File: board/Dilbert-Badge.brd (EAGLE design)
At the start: 53 x 106.7 mm, 27 parts, among them IC1 MCP23017SO, J1 I2C, J2 UART, J6 IO_B, J7 IO_A, SW1 UP, SW2 DOWN, SW3 LEFT, SW4 RIGHT, SW5 A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

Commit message: Update board
[ci skip]
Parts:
- added R5, R6: 10K, adafruit:R0805
- R4: value (none) -> 10K
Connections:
- net LED_OUT renamed NEOPIXEL_OUT
- net N$10 renamed MOSI
- net N$11 renamed MISO
- net N$12 renamed TFT_CS
- net N$9 renamed SCK
- removed net LED_IN: J5.7, LED1.4-DIN, R4.2, X1.10
- new net NEOPIXEL: J5.7, LED1.4-DIN, R6.2, X1.10
- new net TFT_DC: J5.6, R4.1, X1.11
- net 3V3: now also R4.2, R5.2
- net GND: now also R6.1; no longer R4.1
- net GPIO2: no longer J5.6, X1.11
- net SCL: now also R5.1
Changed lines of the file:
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@@
 <element name="R2" library="adafruit" package="R0805" value="10K" x="41.91" y="64.77" rot="R270"/>
 <element name="R3" library="adafruit" package="R0805" value="10K" x="11.43" y="63.5" rot="R90"/>
-<element name="R4" library="adafruit" package="R0805" value="" x="12.7" y="54.61" rot="R90"/>
+<element name="R4" library="adafruit" package="R0805" value="10K" x="12.7" y="54.61" rot="R90"/>
 <element name="C1" library="SparkFun-Capacitors" package="0805-CAP" value="" x="10.16" y="59.69" rot="R90">
 <attribute name="PROD_ID" value="CAP-11330" x="10.16" y="59.69" size="1.778" layer="27" rot="R90" display="off"/>
 </element>
+<element name="R5" library="adafruit" package="R0805" value="10K" x="5.08" y="44.45" rot="R90"/>
+<element name="R6" library="adafruit" package="R0805" value="10K" x="5.08" y="36.83" rot="R270"/>
 </elements>
 <signals>
@@
 <contactref element="IC1" pad="10"/>
 <contactref element="SW8" pad="P$1"/>
-<contactref element="R4" pad="1"/>
 <contactref element="C1" pad="2"/>
+<contactref element="R6" pad="1"/>
 <wire x1="44.83" y1="32.93" x2="49.53" y2="33.02" width="0" layer="19" extent="1-1"/>
 <wire x1="33.4" y1="32.93" x2="44.83" y2="32.93" width="0" layer="19" extent="1-1"/>
@@
 <wire x1="15.24" y1="53.34" x2="16.51" y2="43.89" width="0" layer="19" extent="1-1"/>
 <wire x1="19.17" y1="54" x2="15.24" y2="53.34" width="0" layer="19" extent="16-16"/>
-<wire x1="6.35" y1="55.88" x2="15.24" y2="53.34" width="0" layer="19" extent="1-1"/>
-<wire x1="6.35" y1="59.69" x2="6.35" y2="55.88" width="0" layer="19" extent="1-1"/>
+<wire x1="10.16" y1="60.59" x2="15.24" y2="53.34" width="0" layer="19" extent="1-1"/>
+<wire x1="6.35" y1="59.69" x2="10.16" y2="60.59" width="0" layer="19" extent="1-1"/>
+<wire x1="6.35" y1="55.88" x2="6.35" y2="59.69" width="0" layer="19" extent="1-1"/>
 <wire x1="13.26" y1="21.59" x2="10.54" y2="32.93" width="0" layer="19" extent="1-1"/>
 <wire x1="19.61" y1="16.51" x2="13.26" y2="21.59" width="0" layer="19" extent="1-1"/>
@@
 <wire x1="41.2" y1="20.32" x2="44.83" y2="32.93" width="0" layer="19" extent="1-1"/>
 <wire x1="33.58" y1="12.7" x2="41.2" y2="20.32" width="0" layer="19" extent="1-1"/>
-<wire x1="12.7" y1="53.61" x2="13.26" y2="11.43" width="0" layer="19" extent="1-1"/>
-<wire x1="10.16" y1="60.59" x2="12.7" y2="53.61" width="0" layer="19" extent="1-1"/>
+<wire x1="5.08" y1="37.83" x2="13.26" y2="11.43" width="0" layer="19" extent="1-1"/>
 </signal>
 <signal name="BTN_U">
@@
 <contactref element="IC1" pad="12"/>
 <contactref element="SW8" pad="P$2"/>
+<contactref element="R5" pad="1"/>
 <wire x1="15.24" y1="60.96" x2="19.17" y2="60" width="0" layer="19" extent="16-16"/>
 <wire x1="6.35" y1="48.26" x2="15.24" y2="60.96" width="0" layer="19" extent="1-1"/>
 <wire x1="10.16" y1="37.39" x2="6.35" y2="48.26" width="0" layer="19" extent="1-1"/>
 <wire x1="30.18" y1="34.29" x2="10.16" y2="37.39" width="0" layer="19" extent="16-16"/>
+<wire x1="5.08" y1="43.45" x2="10.16" y2="37.39" width="0" layer="19" extent="1-1"/>
 </signal>
 <signal name="UART_TX">
@@
 <contactref element="J2" pad="1"/>
 </signal>
-<signal name="LED_OUT">
+<signal name="NEOPIXEL_OUT">
 <contactref element="LED4" pad="2-DOUT"/>
 <contactref element="J3" pad="3"/>
 <wire x1="49.53" y1="27.94" x2="44.83" y2="28.03" width="0" layer="19" extent="1-1"/>
 </signal>
-<signal name="LED_IN">
+<signal name="NEOPIXEL">
 <contactref element="LED1" pad="4-DIN"/>
 <contactref element="X1" pad="10"/>
 <contactref element="J5" pad="7"/>
-<contactref element="R4" pad="2"/>
+<contactref element="R6" pad="2"/>
 <wire x1="15.24" y1="55.88" x2="19.17" y2="56" width="0" layer="19" extent="16-16"/>
 <wire x1="7.24" y1="32.93" x2="15.24" y2="55.88" width="0" layer="19" extent="1-1"/>
-<wire x1="12.7" y1="55.61" x2="7.24" y2="32.93" width="0" layer="19" extent="1-1"/>
+<wire x1="5.08" y1="35.83" x2="7.24" y2="32.93" width="0" layer="19" extent="1-1"/>
 </signal>
 <signal name="ESP_ADC">
@@
 <wire x1="38.1" y1="63.5" x2="34.17" y2="62" width="0" layer="19" extent="1-1"/>
 </signal>
-<signal name="N$9">
+<signal name="SCK">
 <contactref element="J4" pad="4"/>
 <contactref element="X1" pad="5"/>
 <wire x1="38.1" y1="60.96" x2="34.17" y2="60" width="0" layer="19" extent="1-1"/>
 </signal>
-<signal name="N$10">
+<signal name="MOSI">
 <contactref element="J4" pad="2"/>
 <contactref element="X1" pad="7"/>
 <wire x1="38.1" y1="55.88" x2="34.17" y2="56" width="0" layer="19" extent="1-1"/>
 </signal>
-<signal name="N$11">
+<signal name="MISO">
 <contactref element="X1" pad="6"/>
 <contactref element="J4" pad="3"/>
 <wire x1="38.1" y1="58.42" x2="34.17" y2="58" width="0" layer="19" extent="1-1"/>
 </signal>
-<signal name="N$12">
+<signal name="TFT_CS">
 <contactref element="X1" pad="14"/>
 <contactref element="J5" pad="3"/>
@@
 </signal>
 <signal name="GPIO2">
-<contactref element="J5" pad="6"/>
-<contactref element="X1" pad="11"/>
 <contactref element="R3" pad="1"/>
-<wire x1="19.17" y1="58" x2="15.24" y2="58.42" width="0" layer="19" extent="16-16"/>
-<wire x1="11.43" y1="62.5" x2="15.24" y2="58.42" width="0" layer="19" extent="1-1"/>
 </signal>
 <signal name="N$14">
@@
 <contactref element="R3" pad="2"/>
 <contactref element="C1" pad="1"/>
+<contactref element="R5" pad="2"/>
+<contactref element="R4" pad="2"/>
+<wire x1="38.1" y1="53.34" x2="41.91" y2="63.77" width="0" layer="19" extent="1-1"/>
 <wire x1="34.17" y1="54" x2="38.1" y2="53.34" width="0" layer="19" extent="16-16"/>
 <wire x1="30.18" y1="38.1" x2="34.17" y2="54" width="0" layer="19" extent="16-16"/>
@@
 <wire x1="49.53" y1="30.48" x2="41.53" y2="28.03" width="0" layer="19" extent="1-1"/>
 <wire x1="18.67" y1="28.03" x2="30.1" y2="28.03" width="0" layer="19" extent="1-1"/>
-<wire x1="7.24" y1="28.03" x2="18.67" y2="28.03" width="0" layer="19" extent="1-1"/>
-<wire x1="6.35" y1="53.34" x2="7.24" y2="28.03" width="0" layer="19" extent="1-1"/>
-<wire x1="6.35" y1="64.77" x2="6.35" y2="53.34" width="0" layer="19" extent="1-1"/>
-<wire x1="12.97" y1="34.29" x2="7.24" y2="28.03" width="0" layer="19" extent="1-1"/>
-<wire x1="41.91" y1="63.77" x2="12.97" y2="34.29" width="0" layer="19" extent="1-1"/>
-<wire x1="11.43" y1="64.5" x2="41.91" y2="63.77" width="0" layer="19" extent="1-1"/>
-<wire x1="10.16" y1="58.79" x2="11.43" y2="64.5" width="0" layer="19" extent="1-1"/>
+<wire x1="12.97" y1="34.29" x2="18.67" y2="28.03" width="0" layer="19" extent="1-1"/>
+<wire x1="7.24" y1="28.03" x2="12.97" y2="34.29" width="0" layer="19" extent="1-1"/>
+<wire x1="6.35" y1="53.34" x2="12.97" y2="34.29" width="0" layer="19" extent="1-1"/>
+<wire x1="10.16" y1="58.79" x2="6.35" y2="53.34" width="0" layer="19" extent="1-1"/>
+<wire x1="12.7" y1="55.61" x2="10.16" y2="58.79" width="0" layer="19" extent="1-1"/>
+<wire x1="11.43" y1="64.5" x2="10.16" y2="58.79" width="0" layer="19" extent="1-1"/>
+<wire x1="6.35" y1="64.77" x2="11.43" y2="64.5" width="0" layer="19" extent="1-1"/>
+<wire x1="5.08" y1="45.45" x2="7.24" y2="28.03" width="0" layer="19" extent="1-1"/>
+</signal>
+<signal name="TFT_DC">
+<contactref element="J5" pad="6"/>
+<contactref element="X1" pad="11"/>
+<contactref element="R4" pad="1"/>
+<wire x1="19.17" y1="58" x2="15.24" y2="58.42" width="0" layer="19" extent="16-16"/>
+<wire x1="12.7" y1="53.61" x2="15.24" y2="58.42" width="0" layer="19" extent="1-1"/>
 </signal>
 </signals>

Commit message: More dev work
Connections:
- net N$7 renamed GPIO16
- net TFT_CS renamed GPIO4
- removed net TFT_DC: J5.6, R4.1, X1.11
- net GPIO2: now also J5.6, R4.1, X1.11
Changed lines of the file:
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@@
 <wire x1="41.91" y1="65.77" x2="34.17" y2="64" width="0" layer="19" extent="1-16"/>
 </signal>
-<signal name="N$7">
+<signal name="GPIO16">
 <contactref element="X1" pad="4"/>
 <contactref element="J4" pad="5"/>
@@
 <wire x1="38.1" y1="58.42" x2="34.17" y2="58" width="0" layer="19" extent="1-1"/>
 </signal>
-<signal name="TFT_CS">
+<signal name="GPIO4">
 <contactref element="X1" pad="14"/>
 <contactref element="J5" pad="3"/>
@@
 <signal name="GPIO2">
 <contactref element="R3" pad="1"/>
+<contactref element="J5" pad="6"/>
+<contactref element="X1" pad="11"/>
+<contactref element="R4" pad="1"/>
+<wire x1="19.17" y1="58" x2="15.24" y2="58.42" width="0" layer="19" extent="16-16"/>
+<wire x1="12.7" y1="53.61" x2="15.24" y2="58.42" width="0" layer="19" extent="1-1"/>
+<wire x1="11.43" y1="62.5" x2="15.24" y2="58.42" width="0" layer="19" extent="1-1"/>
 </signal>
 <signal name="N$14">
@@
 <wire x1="5.08" y1="45.45" x2="7.24" y2="28.03" width="0" layer="19" extent="1-1"/>
 </signal>
-<signal name="TFT_DC">
-<contactref element="J5" pad="6"/>
-<contactref element="X1" pad="11"/>
-<contactref element="R4" pad="1"/>
-<wire x1="19.17" y1="58" x2="15.24" y2="58.42" width="0" layer="19" extent="16-16"/>
-<wire x1="12.7" y1="53.61" x2="15.24" y2="58.42" width="0" layer="19" extent="1-1"/>
-</signal>
 </signals>

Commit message: more work on board
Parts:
- removed J2: UART, SparkFun-Connectors:1X06
- removed J3: (no value), SparkFun-Connectors:1X03
- removed J4: (no value), SparkFun-Connectors:1X08_NO_SILK
- added R7: 10K, adafruit:R0805
- added U$1: 2.2IN_ILI9341, displays:2.2IN_ILI9341
- J1: value I2C -> (none); device SparkFun-Connectors:1X04 -> connectors:10X1_SMD
- J5: value (none) -> I2C; device SparkFun-Connectors:1X08_NO_SILK -> SparkFun-Connectors:1X04
- J6: value IO_B -> UART; device SparkFun-Connectors:1X08_ROUND -> SparkFun-Connectors:1X06
- J7: value IO_A -> NEOPIXEL; device SparkFun-Connectors:1X08_ROUND -> connectors:3X1_SMD
- moved J5 75.2 mm to (61.0, 11.4), turned to 180 degrees
- moved X1 59.7 mm to (81.3, 39.4), turned to 90 degrees
- moved J1 46.8 mm to (52.1, 45.7), flipped to the bottom
- moved J7 39.7 mm to (39.4, 15.2)
- moved J6 38.6 mm to (48.3, 16.5), flipped to the top, turned to 0 degrees
- moved SW8 36.6 mm to (40.6, 61.0), turned to 180 degrees
- moved SW3 29.5 mm to (14.0, 45.7), turned to 270 degrees
- moved SW5 29.3 mm to (8.89, 21.6), turned to 270 degrees
- moved SW2 29.0 mm to (8.89, 39.4), turned to 270 degrees
- moved LED1 27.2 mm to (30.5, 47.0), turned to 180 degrees
- moved IC1 27.1 mm to (52.1, 35.6), flipped to the top
- moved SW6 25.9 mm to (19.1, 15.2), turned to 270 degrees
- moved R6 25.0 mm to (15.2, 59.7)
- moved SW7 25.0 mm to (26.7, 63.5), turned to 180 degrees
- moved R1 23.7 mm to (7.62, 57.1)
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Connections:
- removed net N$14: IC1.1, J6.1
- removed net N$15: IC1.2, J6.2
- removed net N$16: IC1.8, J6.8
- removed net N$17: IC1.7, J6.7
- removed net N$18: IC1.6, J6.6
- removed net N$19: IC1.5, J6.5
- removed net N$20: IC1.4, J6.4
- removed net N$21: IC1.3, J6.3
- removed net N$22: IC1.28, J7.8
- removed net N$23: IC1.27, J7.7
- new net N$10: IC1.8, J1.8
- new net N$11: IC1.7, J1.7
- new net N$12: IC1.6, J1.6
- new net N$13: IC1.5, J1.5
- new net N$4: IC1.1, J1.1
- new net N$5: IC1.2, J1.2
- new net N$6: IC1.3, J1.3
- new net N$7: IC1.4, J1.4
- new net N$8: IC1.28, J1.10
- new net N$9: IC1.27, J1.9
- new net SD_CS: U$1.SD_CS
- new net TFT_BL: U$1.LED
- new net TFT_CS: U$1.CS
- new net TFT_DC: U$1.DC
- new net TFT_RESET: R7.1, U$1.RESET
- net 3V3: now also J5.2, J6.4, J7.2, R7.2, U$1.VCC; no longer J1.2, J2.4, J3.2, J4.1
- net BTN_A: no longer J7.5
- net BTN_B: no longer J7.6
- net BTN_D: no longer J7.2
- net BTN_L: no longer J7.3
- net BTN_R: no longer J7.4
- net BTN_U: no longer J7.1
- net ESP_ADC: no longer J4.7
- net ESP_CH_PD: no longer J4.6
- net GND: now also J5.1, J6.6, J7.1, U$1.GND; no longer J1.1, J2.6, J3.1, J5.8
- net GPIO16: no longer J4.5
- net GPIO2: no longer J5.6
- net GPIO4: no longer J5.3
- net MISO: now also U$1.MISO, U$1.SD_MISO; no longer J4.3
- net MOSI: now also U$1.MOSI, U$1.SD_MOSI; no longer J4.2
- net NEOPIXEL: no longer J5.7
- net NEOPIXEL_OUT: now also J7.3; no longer J3.3
- net RESET: no longer J4.8
- net SCK: now also U$1.SCK, U$1.SD_SCK; no longer J4.4
- net SCL: now also J5.4; no longer J1.4, J5.5
- net SDA: now also J5.3; no longer J1.3, J5.4
- net UART_CTS: now also J6.5; no longer J2.5
- net UART_DTR: now also J6.1; no longer J2.1
- net UART_RX: now also J6.3; no longer J2.3, J5.2
- net UART_TX: now also J6.2; no longer J2.2, J5.1
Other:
- board size 53 x 106.7 mm -> 101.3 x 48.2 mm

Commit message: more work
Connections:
- removed net GPIO16: X1.4
- removed net GPIO4: X1.14
- new net GPIO0: R5.1, SW8.P$2, X1.12
- net SCL: now also X1.13; no longer R5.1, SW8.P$2, X1.12
- net SDA: now also X1.14; no longer X1.13
- net TFT_BL: now also X1.4
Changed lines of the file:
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@@
 </signal>
 <signal name="SDA">
-<contactref element="X1" pad="13"/>
 <contactref element="IC1" pad="13"/>
 <contactref element="J5" pad="3"/>
-<wire x1="47.29" y1="27.94" x2="79.78" y2="46.87" width="0" layer="19" extent="1-16"/>
+<contactref element="X1" pad="14"/>
+<wire x1="47.29" y1="27.94" x2="81.78" y2="46.87" width="0" layer="19" extent="1-16"/>
 <wire x1="55.88" y1="11.43" x2="47.29" y2="27.94" width="0" layer="19" extent="1-1"/>
 </signal>
 <signal name="SCL">
-<contactref element="X1" pad="12"/>
 <contactref element="IC1" pad="12"/>
-<contactref element="SW8" pad="P$2"/>
-<contactref element="R5" pad="1"/>
 <contactref element="J5" pad="4"/>
-<wire x1="47.29" y1="29.21" x2="77.78" y2="46.87" width="0" layer="19" extent="1-16"/>
+<contactref element="X1" pad="13"/>
+<wire x1="47.29" y1="29.21" x2="79.78" y2="46.87" width="0" layer="19" extent="1-16"/>
 <wire x1="53.34" y1="11.43" x2="47.29" y2="29.21" width="0" layer="19" extent="1-1"/>
-<wire x1="43.89" y1="60.96" x2="47.29" y2="29.21" width="0" layer="19" extent="1-1"/>
-<wire x1="5.08" y1="61.23" x2="43.89" y2="60.96" width="0" layer="19" extent="1-1"/>
 </signal>
 <signal name="UART_TX">
@@
 <wire x1="21.32" y1="57.15" x2="81.78" y2="31.87" width="0" layer="19" extent="1-16"/>
 </signal>
-<signal name="GPIO16">
-<contactref element="X1" pad="4"/>
-</signal>
 <signal name="SCK">
 <contactref element="X1" pad="5"/>
@@
 <wire x1="75.78" y1="31.87" x2="101.6" y2="30.48" width="0" layer="19" extent="16-16"/>
 <wire x1="38.1" y1="20.32" x2="75.78" y2="31.87" width="0" layer="19" extent="16-16"/>
-</signal>
-<signal name="GPIO4">
-<contactref element="X1" pad="14"/>
 </signal>
 <signal name="GPIO2">
@@
 <signal name="TFT_BL">
 <contactref element="U$1" pad="LED"/>
+<contactref element="X1" pad="4"/>
+<wire x1="38.1" y1="22.86" x2="79.78" y2="31.87" width="0" layer="19" extent="16-16"/>
 </signal>
 <signal name="TFT_DC">
@@
 <wire x1="52.07" y1="35.56" x2="47.29" y2="38.1" width="0" layer="19" extent="1-1"/>
 </signal>
+<signal name="GPIO0">
+<contactref element="X1" pad="12"/>
+<contactref element="SW8" pad="P$2"/>
+<contactref element="R5" pad="1"/>
+<wire x1="43.89" y1="60.96" x2="77.78" y2="46.87" width="0" layer="19" extent="16-16"/>
+<wire x1="5.08" y1="61.23" x2="43.89" y2="60.96" width="0" layer="19" extent="1-1"/>
+</signal>
 </signals>

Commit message: more neopixels are good
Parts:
- added LED5, LED6, LED7, LED8: WS2812B5050, adafruit:WS2812B
- moved LED4 17.8 mm to (30.5, 31.8)
- moved LED3 14.0 mm to (30.5, 38.1)
- moved LED2 8.89 mm to (30.5, 44.5)
- moved LED1 3.81 mm to (30.5, 50.8)
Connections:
- new net N$16: LED4.2-DOUT, LED5.4-DIN
- new net N$17: LED5.2-DOUT, LED6.4-DIN
- new net N$18: LED6.2-DOUT, LED7.4-DIN
- new net N$19: LED7.2-DOUT, LED8.4-DIN
- new net VDD: LED2.1-VDD, LED3.1-VDD, LED4.1-VDD, LED5.1-VDD, LED6.1-VDD, LED7.1-VDD
- net 3V3: now also LED8.1-VDD; no longer LED2.1-VDD, LED3.1-VDD, LED4.1-VDD
- net GND: now also LED5.3-GND, LED6.3-GND, LED7.3-GND, LED8.3-GND
- net NEOPIXEL_OUT: now also LED8.2-DOUT; no longer LED4.2-DOUT

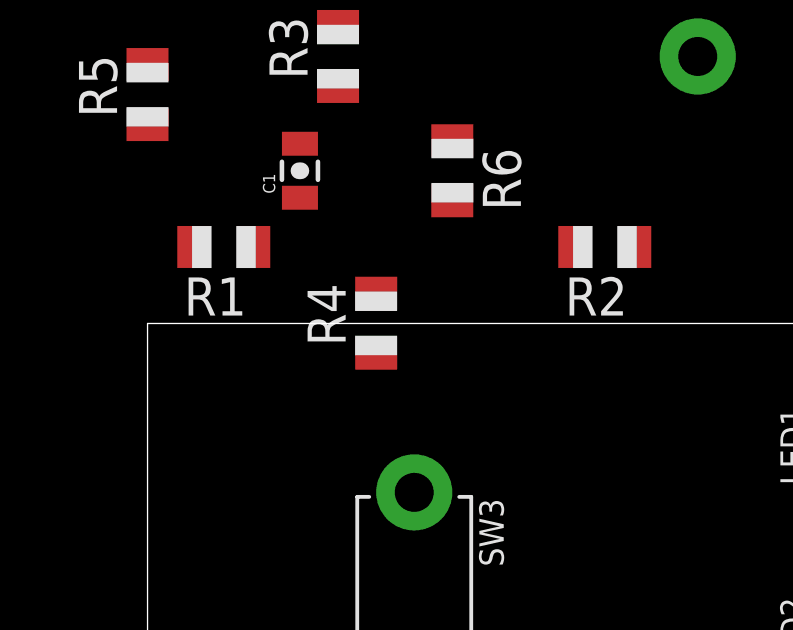
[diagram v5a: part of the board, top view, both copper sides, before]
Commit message: switch to hardware SPI with i2c port expander
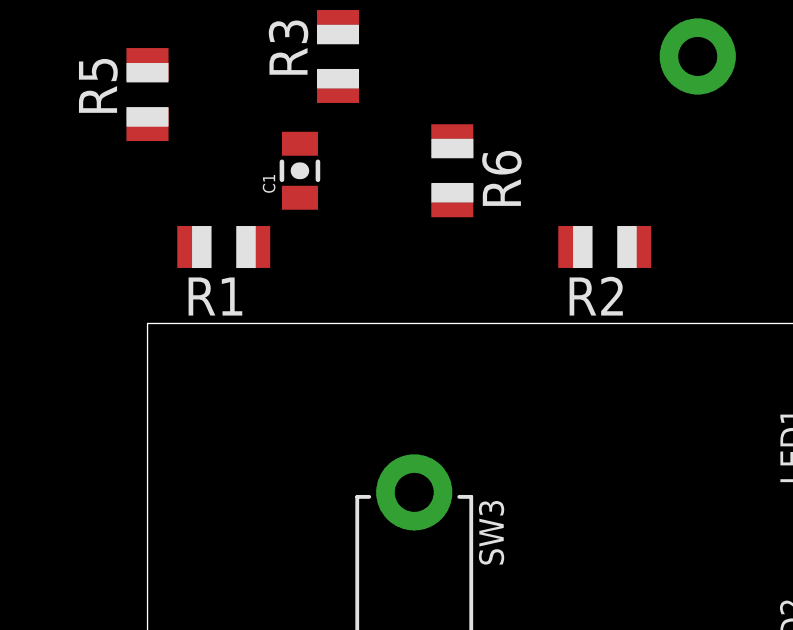
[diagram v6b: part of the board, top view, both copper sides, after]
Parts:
- removed R4: 10K, adafruit:R0805
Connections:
- removed net GPIO0: R5.1, SW8.P$2, X1.12
- removed net GPIO2: R3.1, R4.1, X1.11
- net 3V3: no longer R4.2
- net TFT_CS: now also R5.1, SW8.P$2, X1.12
- net TFT_DC: now also R3.1, X1.11
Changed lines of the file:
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@@
 <element name="R2" library="adafruit" package="R0805" value="10K" x="20.32" y="57.15" rot="R180"/>
 <element name="R3" library="adafruit" package="R0805" value="10K" x="11.43" y="63.5" rot="R90"/>
-<element name="R4" library="adafruit" package="R0805" value="10K" x="12.7" y="54.61" rot="R90"/>
 <element name="C1" library="SparkFun-Capacitors" package="0805-CAP" value="" x="10.16" y="59.69" rot="R90">
 <attribute name="PROD_ID" value="CAP-11330" x="10.16" y="59.69" size="1.778" layer="27" rot="R90" display="off"/>
@@
 <wire x1="38.1" y1="20.32" x2="75.78" y2="31.87" width="0" layer="19" extent="16-16"/>
 </signal>
-<signal name="GPIO2">
-<contactref element="R3" pad="1"/>
-<contactref element="X1" pad="11"/>
-<contactref element="R4" pad="1"/>
-<wire x1="12.7" y1="53.61" x2="75.78" y2="46.87" width="0" layer="19" extent="1-16"/>
-<wire x1="11.43" y1="62.5" x2="12.7" y2="53.61" width="0" layer="19" extent="1-1"/>
-</signal>
 <signal name="3V3">
 <contactref element="R1" pad="2"/>
@@
 <contactref element="C1" pad="1"/>
 <contactref element="R5" pad="2"/>
-<contactref element="R4" pad="2"/>
 <contactref element="U$1" pad="VCC"/>
 <contactref element="R7" pad="2"/>
@@
 <wire x1="58.42" y1="11.43" x2="55.88" y2="16.51" width="0" layer="19" extent="1-1"/>
 <wire x1="39.37" y1="12.7" x2="55.88" y2="16.51" width="0" layer="19" extent="16-16"/>
+<wire x1="28.03" y1="8" x2="39.37" y2="12.7" width="0" layer="19" extent="1-16"/>
 <wire x1="47.29" y1="33.02" x2="55.88" y2="16.51" width="0" layer="19" extent="1-1"/>
 <wire x1="41.91" y1="35.29" x2="47.29" y2="33.02" width="0" layer="19" extent="1-1"/>
@@
 <wire x1="28.03" y1="52.45" x2="38.1" y2="40.64" width="0" layer="19" extent="1-1"/>
 <wire x1="19.32" y1="57.15" x2="28.03" y2="52.45" width="0" layer="19" extent="1-1"/>
-<wire x1="12.7" y1="55.61" x2="19.32" y2="57.15" width="0" layer="19" extent="1-1"/>
-<wire x1="10.16" y1="58.79" x2="12.7" y2="55.61" width="0" layer="19" extent="1-1"/>
+<wire x1="10.16" y1="58.79" x2="19.32" y2="57.15" width="0" layer="19" extent="1-1"/>
 <wire x1="6.62" y1="57.15" x2="10.16" y2="58.79" width="0" layer="19" extent="1-1"/>
 <wire x1="11.43" y1="64.5" x2="10.16" y2="58.79" width="0" layer="19" extent="1-1"/>
 <wire x1="5.08" y1="63.23" x2="6.62" y2="57.15" width="0" layer="19" extent="1-1"/>
-<wire x1="28.03" y1="8" x2="39.37" y2="12.7" width="0" layer="19" extent="1-16"/>
 </signal>
 <signal name="TFT_BL">
@@
 <signal name="TFT_DC">
 <contactref element="U$1" pad="DC"/>
+<contactref element="R3" pad="1"/>
+<contactref element="X1" pad="11"/>
+<wire x1="38.1" y1="30.48" x2="75.78" y2="46.87" width="0" layer="19" extent="16-16"/>
+<wire x1="11.43" y1="62.5" x2="38.1" y2="30.48" width="0" layer="19" extent="1-1"/>
 </signal>
 <signal name="TFT_RESET">
@@
 <signal name="TFT_CS">
 <contactref element="U$1" pad="CS"/>
+<contactref element="X1" pad="12"/>
+<contactref element="SW8" pad="P$2"/>
+<contactref element="R5" pad="1"/>
+<wire x1="43.89" y1="60.96" x2="77.78" y2="46.87" width="0" layer="19" extent="16-16"/>
+<wire x1="38.1" y1="35.56" x2="43.89" y2="60.96" width="0" layer="19" extent="1-1"/>
+<wire x1="5.08" y1="61.23" x2="43.89" y2="60.96" width="0" layer="19" extent="1-1"/>
 </signal>
 <signal name="SD_CS">
@@
 <wire x1="52.07" y1="35.56" x2="47.29" y2="38.1" width="0" layer="19" extent="1-1"/>
 </signal>
-<signal name="GPIO0">
-<contactref element="X1" pad="12"/>
-<contactref element="SW8" pad="P$2"/>
-<contactref element="R5" pad="1"/>
-<wire x1="43.89" y1="60.96" x2="77.78" y2="46.87" width="0" layer="19" extent="16-16"/>
-<wire x1="5.08" y1="61.23" x2="43.89" y2="60.96" width="0" layer="19" extent="1-1"/>
-</signal>
 <signal name="VDD">
